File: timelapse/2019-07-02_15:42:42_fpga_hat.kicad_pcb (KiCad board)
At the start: 4 copper layers, 65 x 56.5 mm, 90 parts, among them J1 2x20, J2 AudioJack3, J3 Conn_02x06_Top_Bottom, J4 Conn_02x06_Top_Bottom, J5 Conn_02x06_Top_Bottom, J6 Conn_01x02, SW1 PTS815, SW2 PTS815, SW3 PTS815, SW4 PTS815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

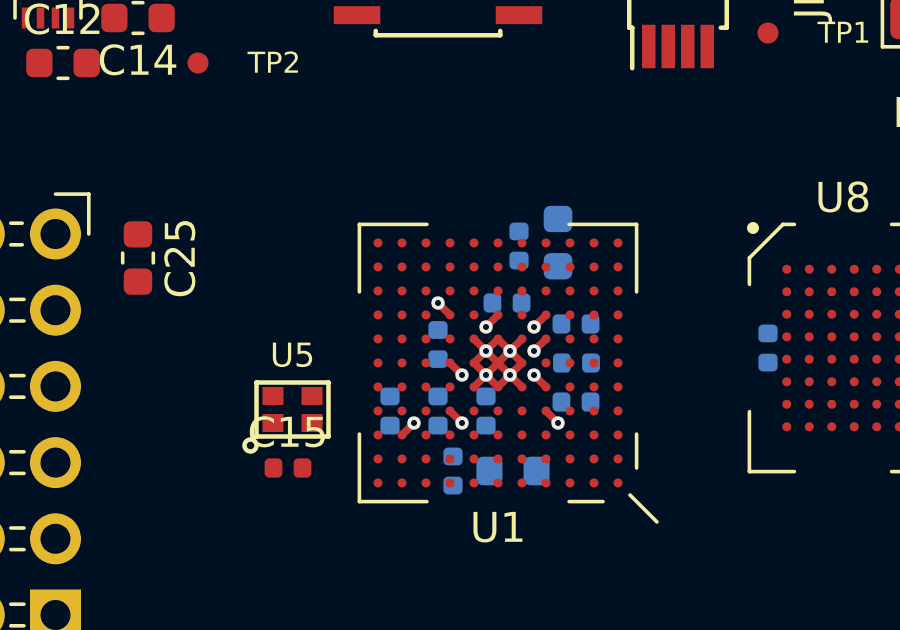
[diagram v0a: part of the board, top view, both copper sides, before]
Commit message: First run at power planes under FPGA
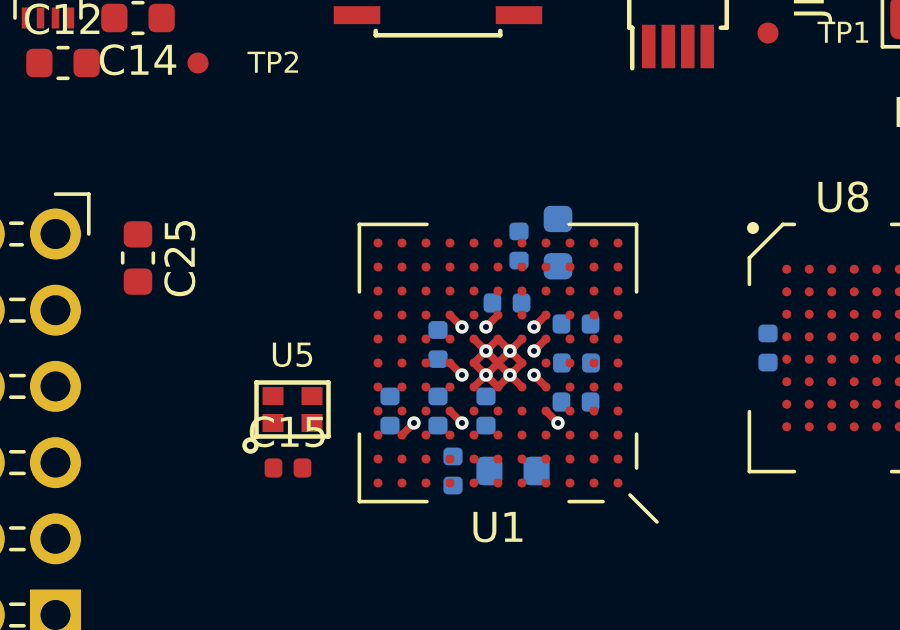
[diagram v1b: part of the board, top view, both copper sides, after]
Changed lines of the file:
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@@
     (solder_mask_min_width 0.1)
     (aux_axis_origin 0 0)
-    (visible_elements FFFFF77F)
+    (visible_elements FFFFFF7F)
     (pcbplotparams
       (layerselection 0x010fc_ffffffff)
@@
   (segment (start 132.9 106.1) (end 133.3 106.5) (width 0.25) (layer F.Cu) (net 1))
   (segment (start 132.1 106.1) (end 132.5 106.5) (width 0.25) (layer F.Cu) (net 1))
+  (via (at 131.3 105.3) (size 0.45) (drill 0.2) (layers F.Cu B.Cu) (net 2))
+  (segment (start 130.9 104.9) (end 131.3 105.3) (width 0.25) (layer F.Cu) (net 2))
   (via (at 133.7 105.3) (size 0.45) (drill 0.2) (layers F.Cu B.Cu) (net 2))
   (segment (start 134.1 104.9) (end 133.7 105.3) (width 0.25) (layer F.Cu) (net 2))
@@
   (segment (start 130.9 108.1) (end 131.3 108.5) (width 0.25) (layer F.Cu) (net 2))
   (via (at 131.3 108.5) (size 0.45) (drill 0.2) (layers F.Cu B.Cu) (net 2))
-  (via (at 130.5 104.5) (size 0.45) (drill 0.2) (layers F.Cu B.Cu) (net 2))
-  (segment (start 130.9 104.9) (end 130.5 104.5) (width 0.25) (layer F.Cu) (net 2))
   (via (at 131.3 106.9) (size 0.45) (drill 0.2) (layers F.Cu B.Cu) (net 7))
   (segment (start 130.9 106.5) (end 131.3 106.9) (width 0.25) (layer F.Cu) (net 7))
@@
     (polygon
       (pts
-        (xy 134.6 105.1) (xy 134.1 105.6) (xy 133.6 105.6) (xy 132.9 104.9) (xy 131.9 104.9)
-        (xy 131.2 104.9) (xy 130.9 105.2) (xy 130.9 105.5) (xy 130.9 106.1) (xy 130.9 107.4)
+        (xy 134.6 105.1) (xy 134 105.7) (xy 133.2 105.7) (xy 132.4 104.9) (xy 131.9 104.9)
+        (xy 131.7 105.1) (xy 131.7 105.3) (xy 131.4 105.6) (xy 130.9 106.1) (xy 130.9 107.4)
         (xy 132.2 108.7) (xy 133.8 108.7) (xy 134.4 108.1) (xy 134.7 108.1) (xy 135.1 108.5)
         (xy 135.1 109.2) (xy 134.7 109.6) (xy 131.6 109.6) (xy 129.7 107.7) (xy 119.9 97.9)
